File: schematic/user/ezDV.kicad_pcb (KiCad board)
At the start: 4 copper layers, 64.8 x 69.9 mm, 98 parts, among them J1 TYPE-C-31-M-04, J10 Radio Audio, J2 Radio_Jack, J3 User_Jack, J4 I2C Breakout, J5 PTT Breakout, J6 ESP32_UART0, J7 MCU Power, J8 ULP Serial, J9 User Audio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

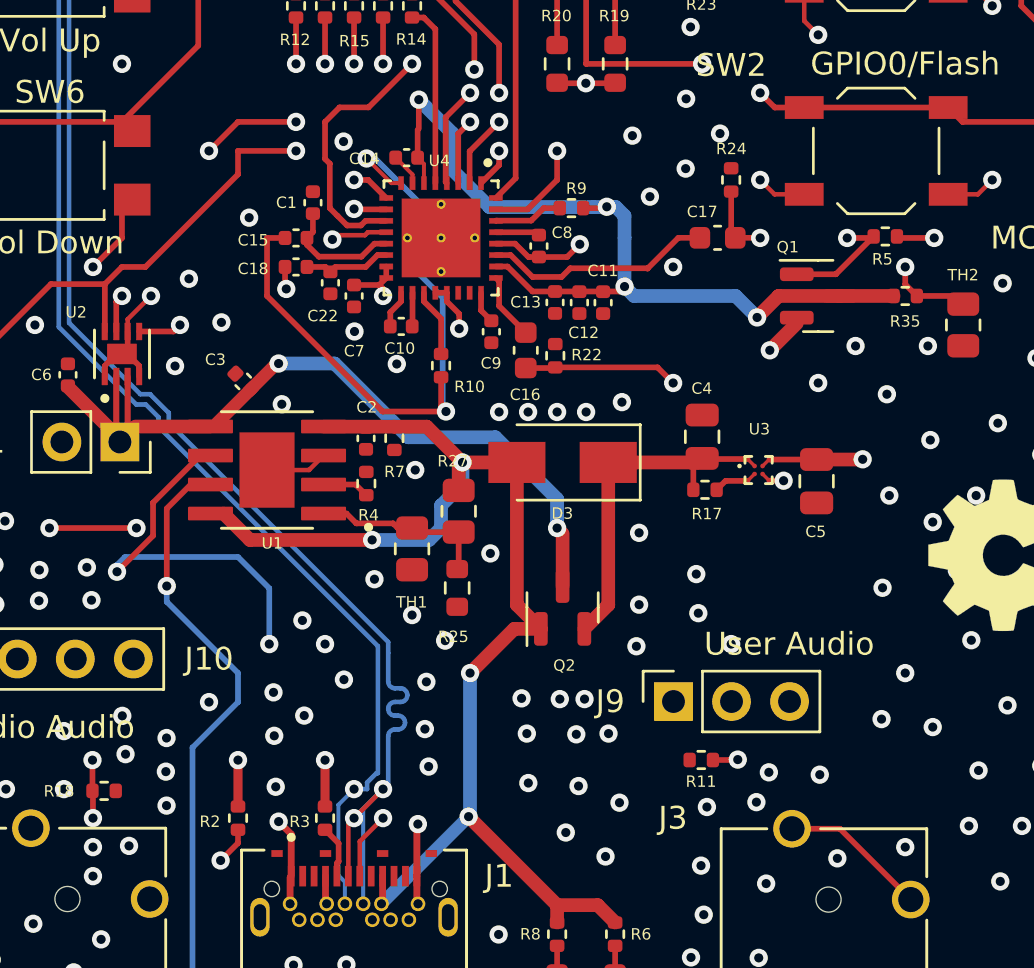
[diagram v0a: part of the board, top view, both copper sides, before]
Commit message: v0.6 board: minor tweaks in routing to reduce crosstalk.
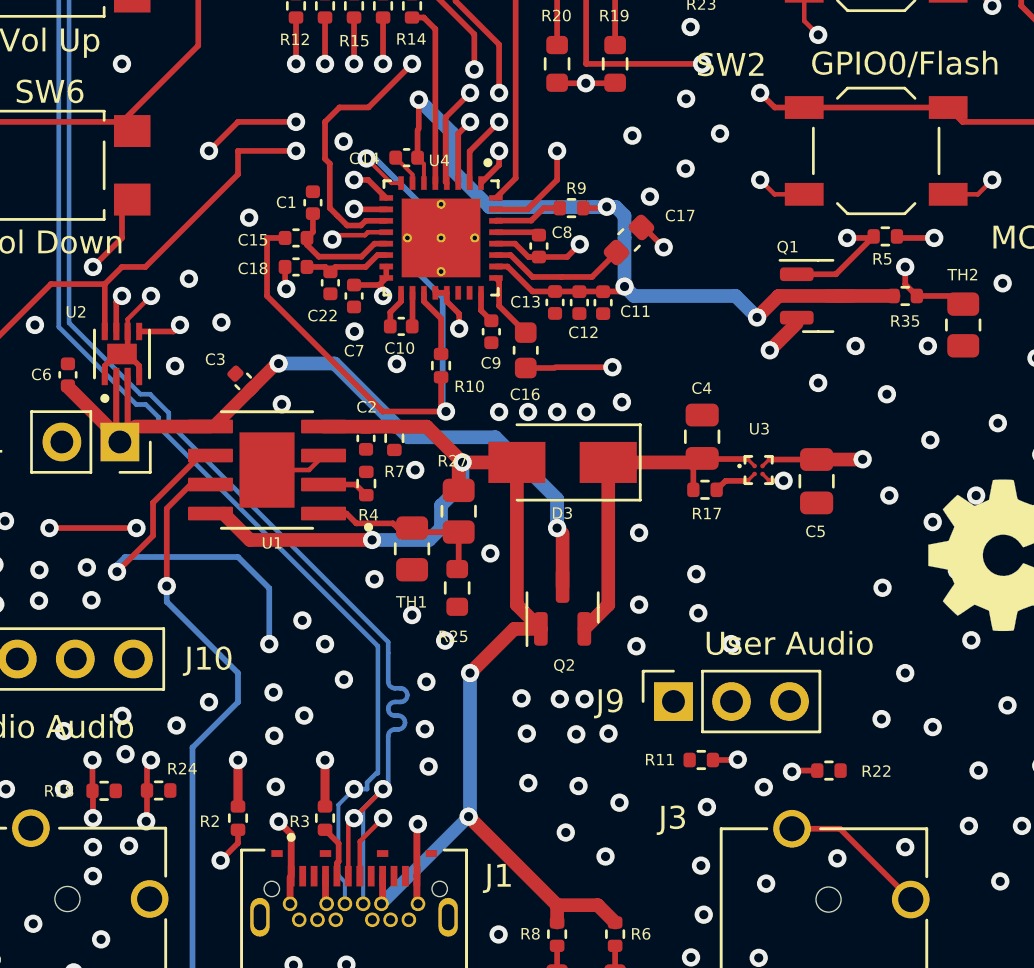
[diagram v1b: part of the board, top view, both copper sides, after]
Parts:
- moved R24 36.6 mm to (61.3, 125.8), turned to 180 degrees
- moved R22 21.8 mm to (90.6, 124.9), turned to 0 degrees
- moved C17 3.88 mm to (81.9, 101.7), turned to 45 degrees
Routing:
- net Radio_Jack_Speaker: track 52.0 -> 47.1 mm, vias 1 -> 3
- net TLV320_OUT_RADIO: track 10.0 -> 6.12 mm
- net Radio_Jack_Mic: track 42.1 -> 41.6 mm
- net User_Jack_Speaker: track 35.2 -> 34.9 mm, vias 1 -> 2
- net GND: vias 211 -> 206

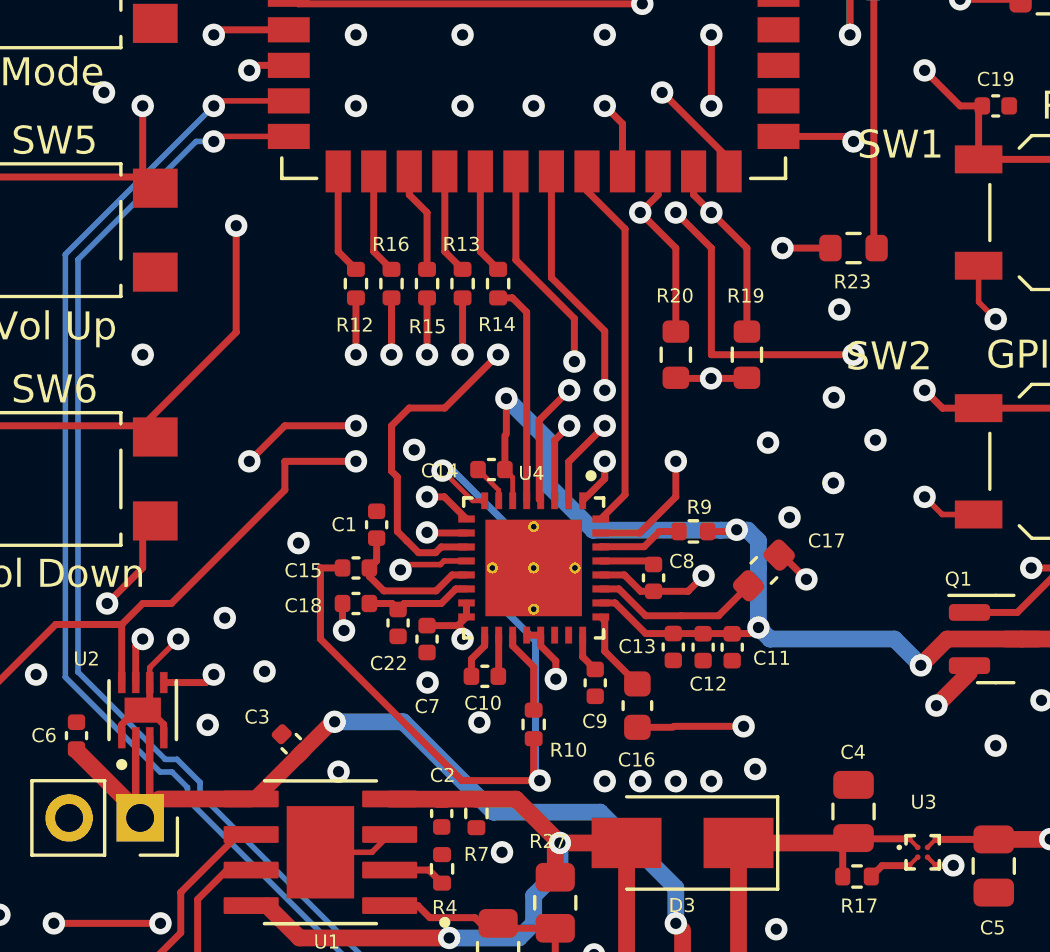
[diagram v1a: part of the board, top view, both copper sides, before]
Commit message: v0.6 board: more tweaking of capacitors and traces.
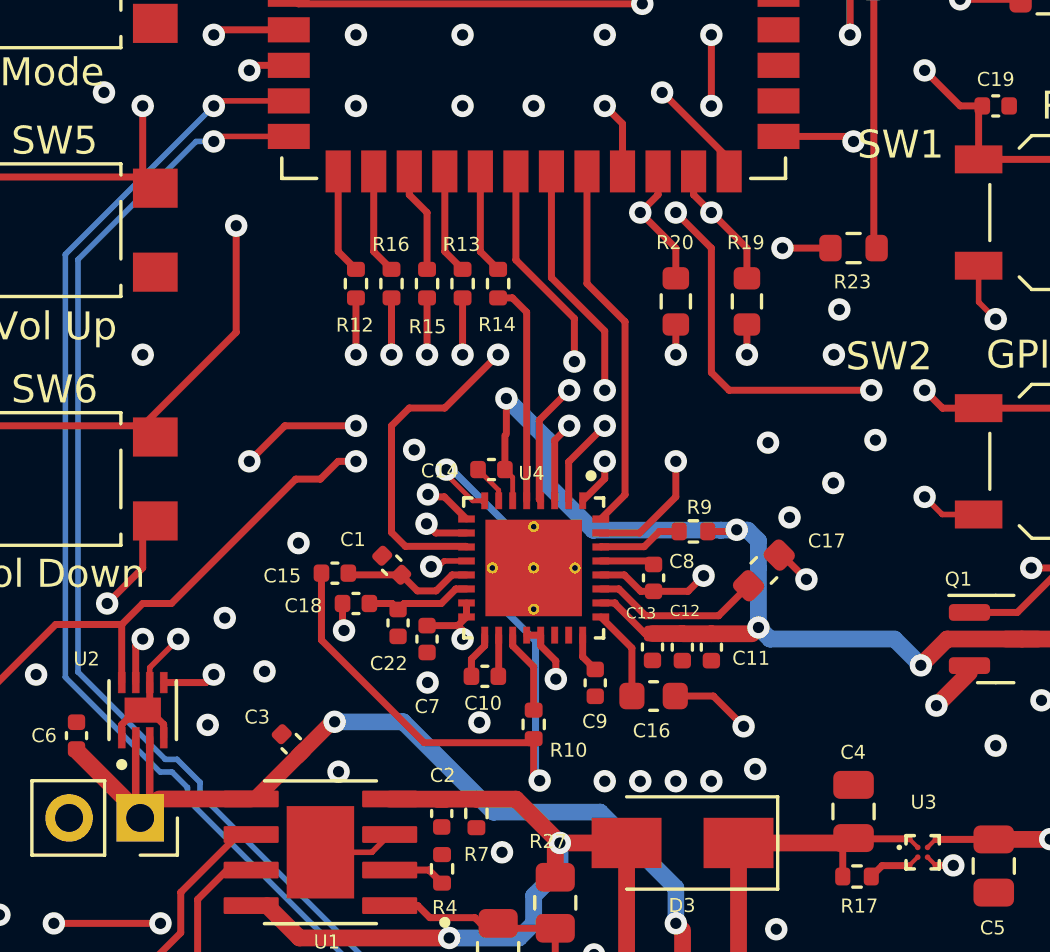
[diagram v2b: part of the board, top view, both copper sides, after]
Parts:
- moved R19 1.91 mm to (81.3, 92.1)
- moved R20 1.91 mm to (78.7, 92.1)
- moved C1 1.54 mm to (68.6, 101.5), turned to 135 degrees
- moved C15 0.78 mm to (66.6, 101.8)
- moved C13 0.74 mm to (77.9, 104.4)
- moved C11 0.74 mm to (80.0, 104.4)
- moved C12 0.74 mm to (79.0, 104.4)
- moved C16 0.67 mm to (77.9, 106.2), turned to 0 degrees
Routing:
- net GPIO47_SDA: track 55.5 -> 53.2 mm
- net GPIO48_SCL: track 58.4 -> 56.5 mm
- net TLV320_IN_DETECT: track 65.7 -> 64.0 mm
- net GND: track 82.1 -> 80.6 mm
- net User_Jack_Speaker: track 34.9 -> 34.0 mm
- net TLV320_IN_USER: track 5.40 -> 4.73 mm
- net 3.3V_PERIPH: track 137.3 -> 137.8 mm, vias 6 -> 7

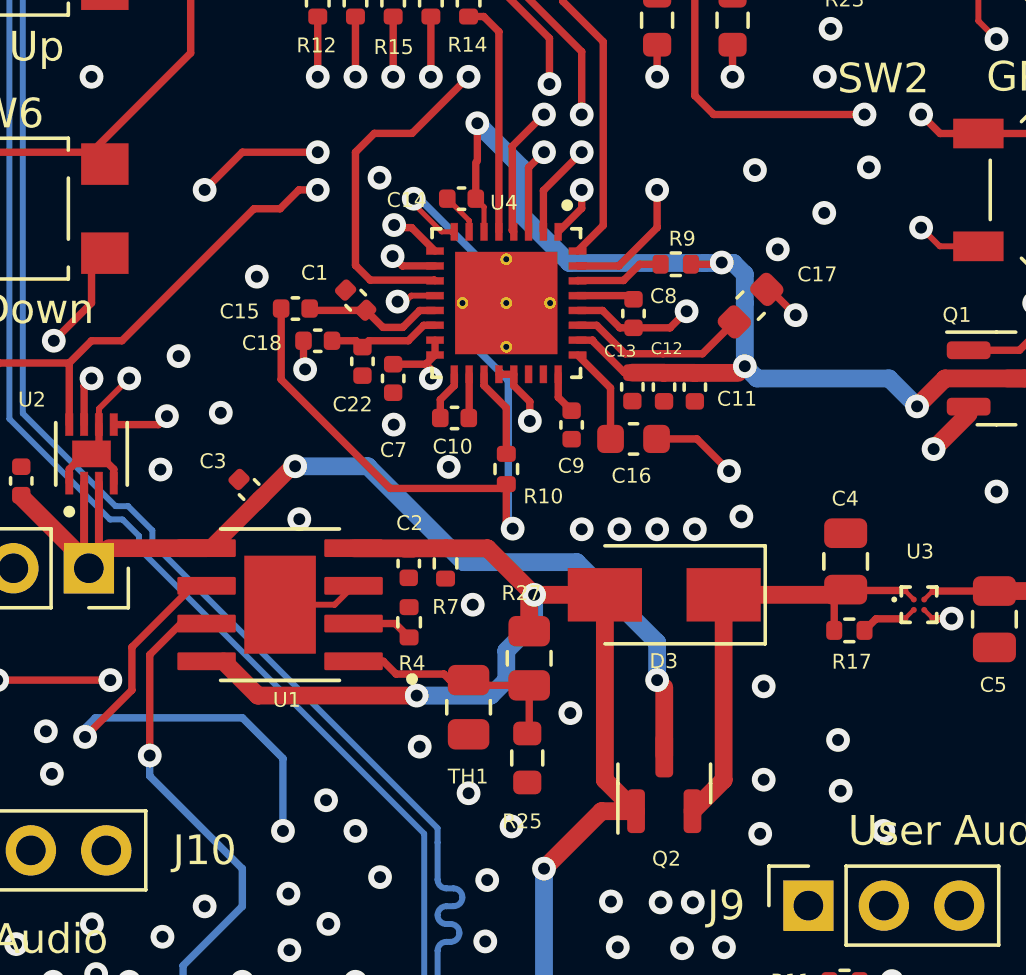
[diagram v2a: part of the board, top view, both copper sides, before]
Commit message: v0.6 board: more tweaking of traces.
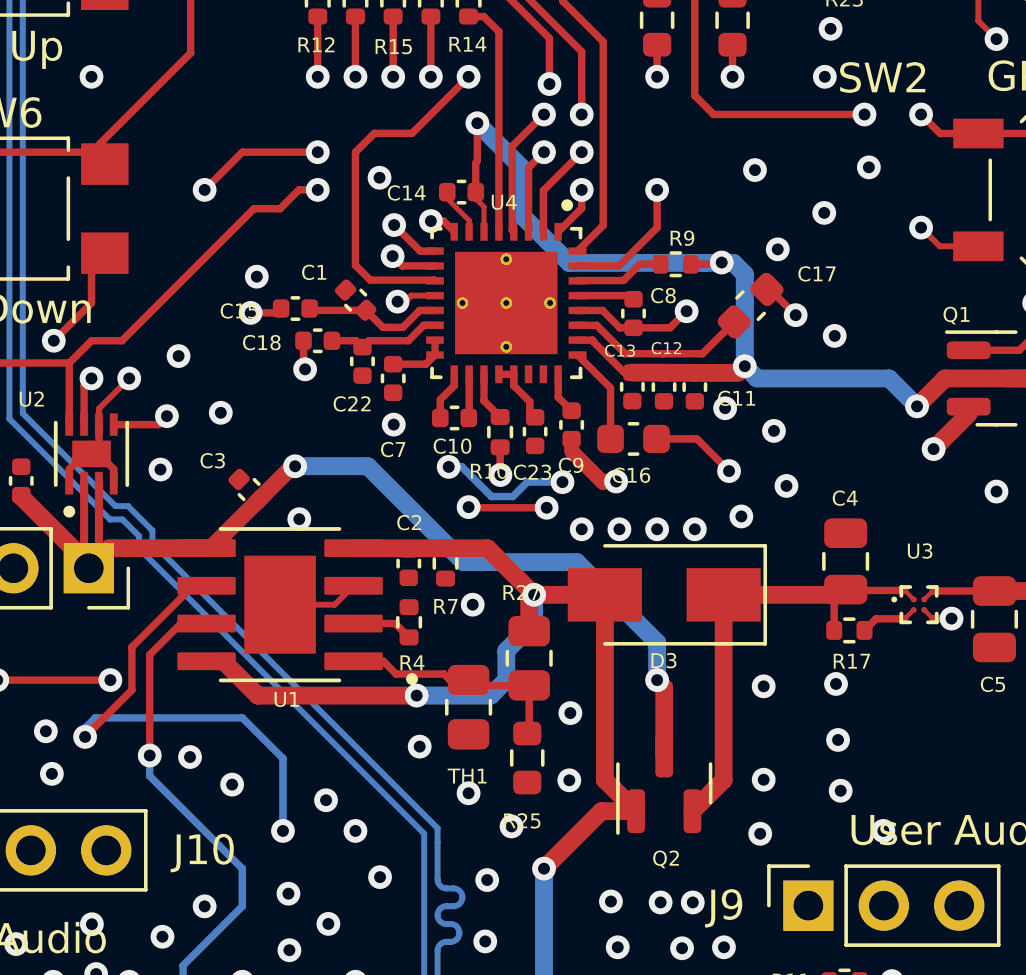
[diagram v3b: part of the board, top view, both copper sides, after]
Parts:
- added C23: 0.1uF, Capacitor_SMD:C_0402_1005Metric, F.Cu at (74.6, 105.9)
- moved R10 1.26 mm to (73.5, 105.9)
- moved C14 0.22 mm to (72.2, 97.9)
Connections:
- C7 pad 1: Net-(C7-Pad1) -> Net-(U4-Pad15)
- U4 pad 15: Net-(C7-Pad1) -> Net-(U4-Pad15)
- U4 pad 16: Net-(C7-Pad1) -> Net-(U4-Pad15)
- U4 pad 20: Net-(C7-Pad1) -> Net-(U4-Pad20)
- U4 pad 21: Net-(C7-Pad1) -> Net-(U4-Pad20)
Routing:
- net Net-(C7-Pad1): track 8.81 -> 0.00 mm, vias 2 -> 0
- net TLV320_IN_DETECT: track 64.0 -> 59.1 mm, vias 3 -> 4
- net GND: track 80.6 -> 83.0 mm, vias 206 -> 214
- net Net-(U4-Pad20): track 0.00 -> 2.25 mm
- net Net-(U4-Pad15): track 0.00 -> 2.04 mm
- net GPIO47_SDA: track 53.2 -> 54.7 mm
- net TLV320_OUT_MICBIAS: track 2.99 -> 1.66 mm
- net Radio_Jack_PTT: track 88.1 -> 88.6 mm, vias 5 -> 7
- net Radio_Jack_Speaker: vias 3 -> 5

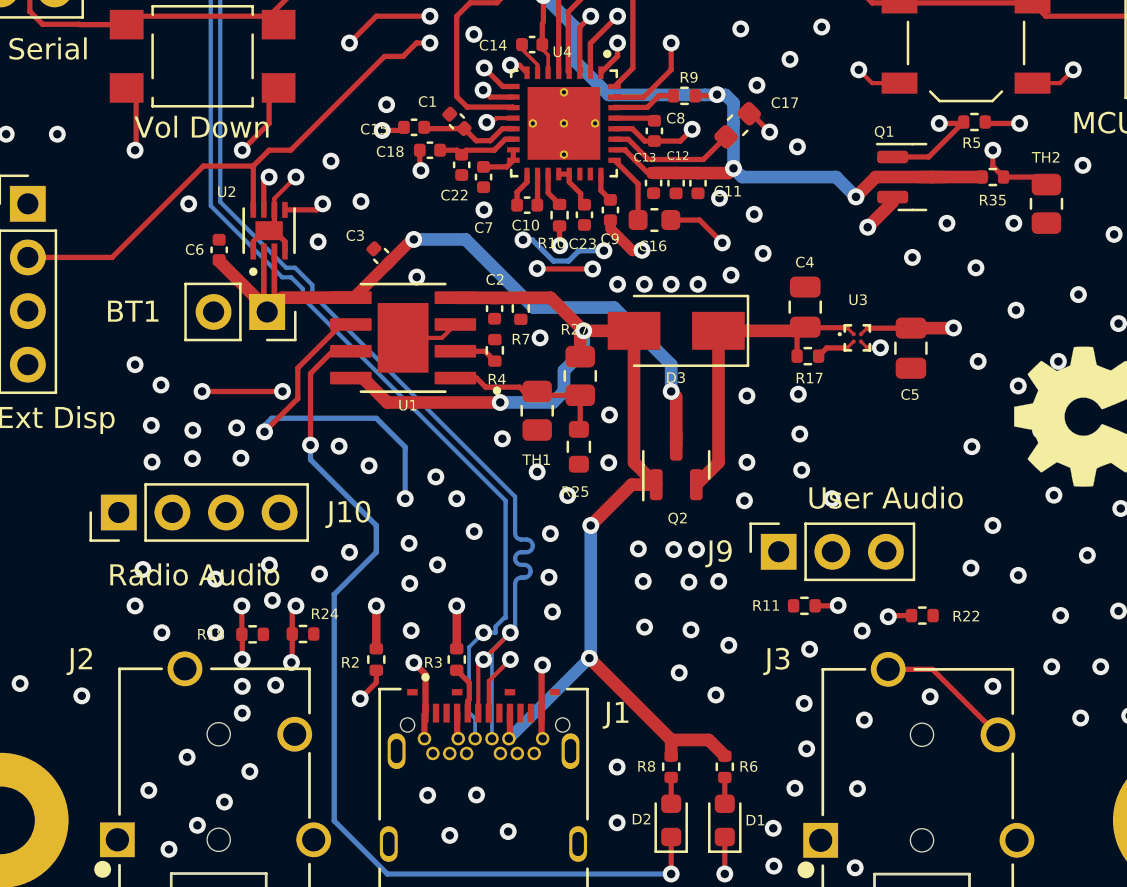
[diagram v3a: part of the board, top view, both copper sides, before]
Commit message: v0.6 board: additional tweaks.
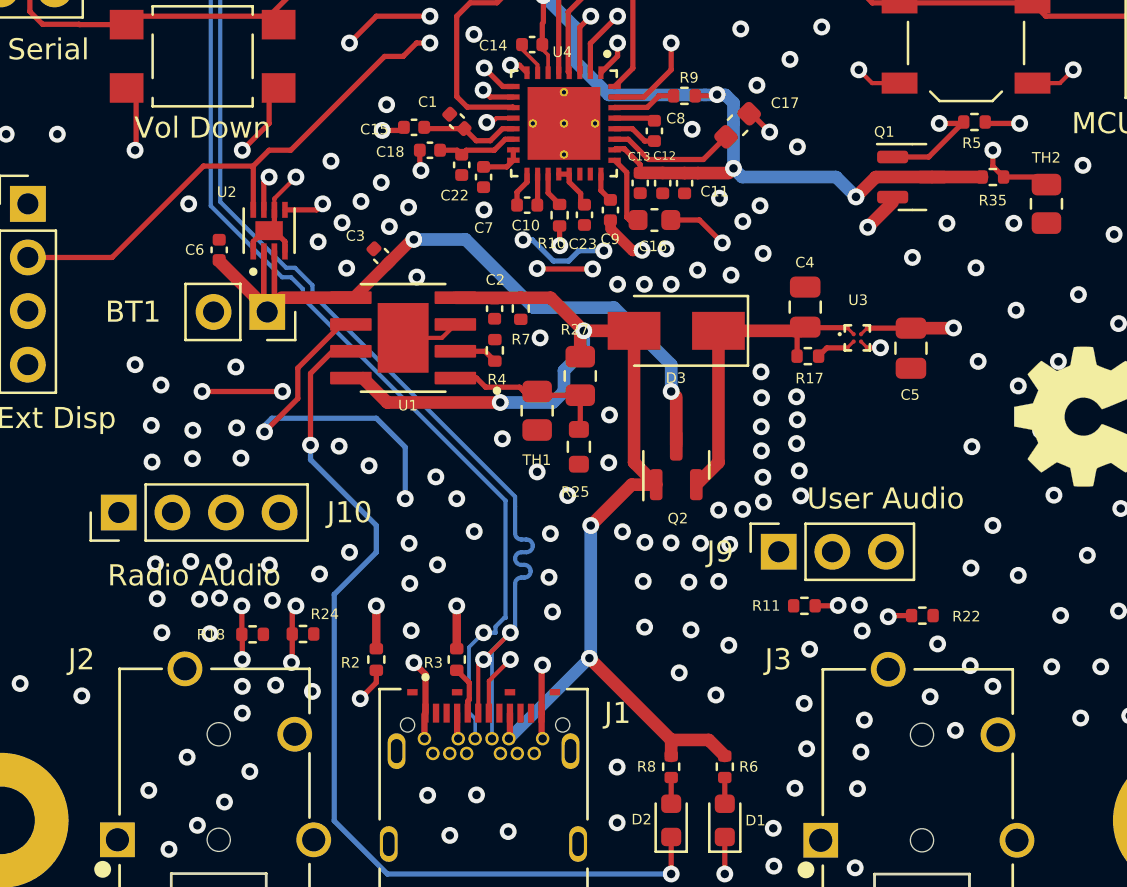
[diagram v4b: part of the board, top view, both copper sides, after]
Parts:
- moved C11 0.64 mm to (79.4, 104.4)
- moved C12 0.64 mm to (78.3, 104.4)
- moved C13 0.63 mm to (77.3, 104.4)
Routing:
- net GND: track 83.0 -> 81.0 mm, vias 214 -> 239

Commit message: v0.6 board: use 2.2K for microphone bias resistor.
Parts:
- R10: value 2.7K -> 2.2K
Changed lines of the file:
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@@
       (effects (font (size 0.5 0.5) (thickness 0.125)))
     )
-    (fp_text value "2.7K" (at 0 1.17 90) (layer "F.Fab")
+    (fp_text value "2.2K" (at 0 1.17 90) (layer "F.Fab")
       (effects (font (size 1 1) (thickness 0.15)))
     )
